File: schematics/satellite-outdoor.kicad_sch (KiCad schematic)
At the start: 3 parts, among them U1 LPS22HB, U2 AHT20

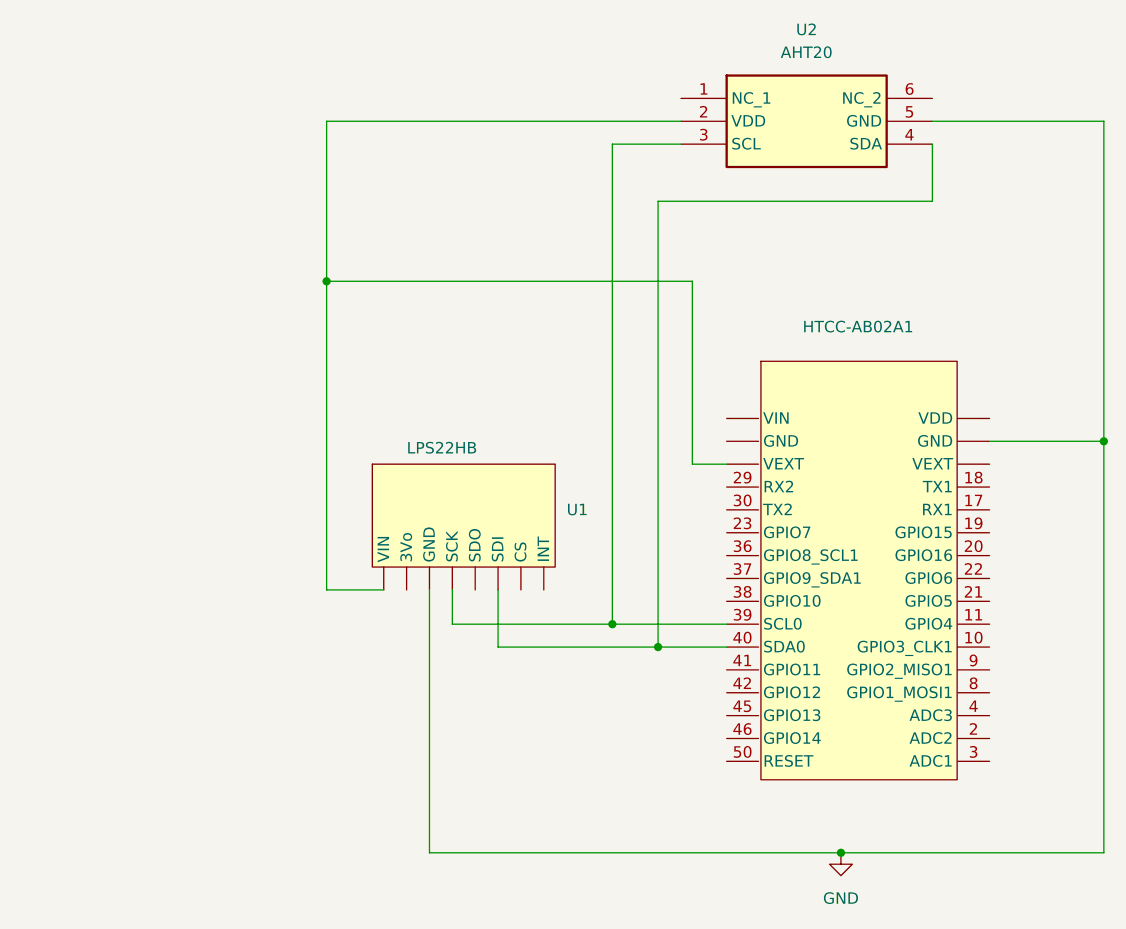
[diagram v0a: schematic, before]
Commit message: Schematics/ add i2c pullups on outdoor sat.
20ko should do the trick.
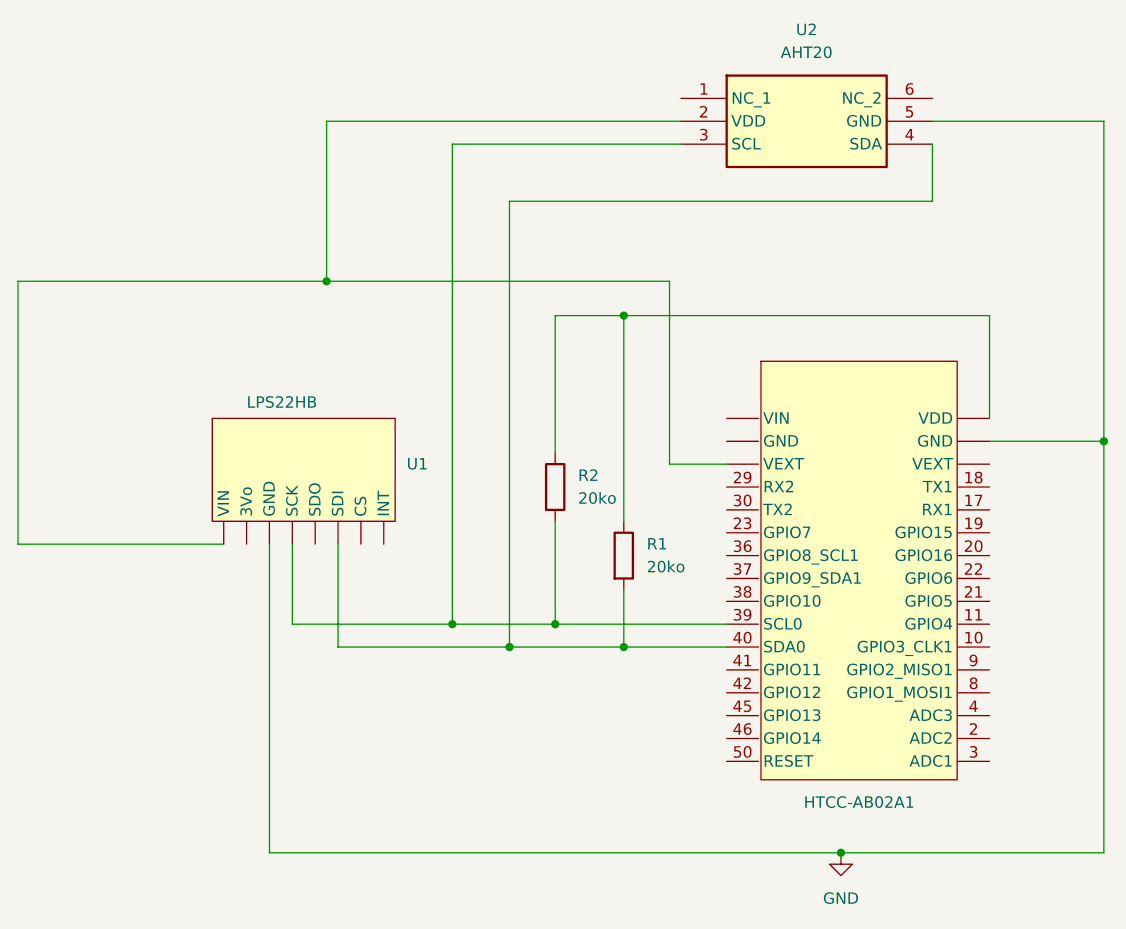
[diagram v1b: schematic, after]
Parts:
- added R1, R2: 20ko, symbol Device:R
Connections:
- net at HTCC-AB02A1.39 (SCL0), U1. (VIN), U2.3 (SCL): now also R2.2
- net at HTCC-AB02A1.40 (SDA0), U1. (VIN), U2.4 (SDA): now also R1.2
- new net: HTCC-AB02A1. (VIN), U1. (VIN), U2.2 (VDD)
- new net: HTCC-AB02A1. (VIN), R1.1, R2.1
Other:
- moved on the sheet: U1
